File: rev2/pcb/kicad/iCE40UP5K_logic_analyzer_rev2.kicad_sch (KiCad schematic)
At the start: 117 parts, among them IC1 ICE40UP5K-SG48I, IC2 MIC5504-3.3YM5-TR, IC3 MIC5504-1.2YM5-TR, IC4 CP2102N-A02-GQFN24, IC5 W25Q40CLSNIG, IC6 SN74LVC14ADBRE4, IC7 SN74LVC14ADBRE4, IC8 SN74LVC14ADBRE4, J1 USB B Female Connector, J2 61300611121, J3 61202021621

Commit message: USB-UART bridge IC implementation. added LC filter to VPHY and VPLL. added caps to remaining power pins.
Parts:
- removed IC4: CP2102N-A02-GQFN24, UART_USB_bridge_CP2102N-A02-GQFN24:QFN50P400X400X80-25N-D, symbol UART_USB_bridge_CP2102N-A02-GQFN24:CP2102N-A02-GQFN24
- removed R8: 10k, Resistor_SMD:R_0603_1608Metric, symbol Device:R
- removed TP12, TP15: GND, TestPoint:TestPoint_Pad_D1.0mm, symbol Connector:TestPoint
- removed TP7: SPI_SCK, TestPoint:TestPoint_Pad_D1.0mm, symbol Connector:TestPoint
- removed TP8: FPGA_UART_TX, TestPoint:TestPoint_Pad_D1.0mm, symbol Connector:TestPoint
- removed TP9: FPGA_UART_RX, TestPoint:TestPoint_Pad_D1.0mm, symbol Connector:TestPoint
- added C27, C28, C29, C30, C31, C32, C33: 0u1, 0u1_0603_cap_C0603C104M4RAC:CAPC1608X95N, symbol Device:C
- added C34, C35: 4u7, 4u7_0805_cap_C0805C475K4RACTM:C0805, symbol Device:C
- added D8: USB_RX, Blue_LED_0805_APT2012LVBC/D:LEDC2012X85N, symbol Device:LED
- added D9: USB_TX, Yellow_LED_0805_150080YS75000:LEDC2012X70N, symbol Device:LED
- added FB1, FB2: BLM18AG601SN1D, BLM18SP221SN1B, symbol Ferrite_bead_BLM18AG601SN1D:BLM18AG601SN1D
- added IC4: FT2232HL-TRAY, QFP50P1200X1200X160-64N, symbol UART_USB_bridge_FT2232HL:FT2232HL-TRAY
- C6: value 4u7 -> 3u3
- R2: value 1k -> 12k
- R3: value 22k1 -> 10k
- R4: value 47k5 -> 4k7
- R5: value 10k -> 1k
- R6: value 10k -> 470R
- R7: value 10k -> 680R
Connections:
- net +3V3: now also R6.1, C28.2, C29.2, C30.1, C31.1, FB1.2, FB2.1, IC4.20 (VCCIO_1), IC4.31 (VCCIO_2), IC4.42 (VCCIO_3), IC4.50 (VREGIN), IC4.56 (VCCIO_4); no longer C6.1, C7.1, C8.1, R2.1, R6.2
- net +5V: now also R4.2; no longer R3.1
- net GND: now also R2.2, R3.1, C27.2, C28.1, C29.1, C30.2, C31.2, C32.1, C33.1, C34.2, C35.2, IC4.1 (GND_1), IC4.10 (AGND), IC4.11 (GND_3), IC4.13 (TEST), IC4.15 (GND_4), IC4.25 (GND_5), IC4.35 (GND_6), IC4.47 (GND_7), IC4.5 (GND_2), IC4.51 (GND_8), IC4.60 (PWREN#); no longer R4.2
- net at R5.2: now also IC4.14 (RESET#)
- net RTS#: now reaches IC1.2 (IOB_6A)
- net RTS#: now also IC4.18 (ADBUS2)
- net FPGA_UART_RX: now reaches IC1.3 (IOB_9B)
- net FPGA_UART_RX: now also IC4.16 (ADBUS0)
- net FPGA_UART_TX: now reaches IC1.4 (IOB_8A)
- net FPGA_UART_TX: now also IC4.17 (ADBUS1)
- net CTS#: now reaches IC1.6 (IOB_13B)
- net CTS#: now also IC4.19 (ADBUS3)
- net at R3.2, R4.1: now also IC4.59 (BCBUS7)
- net at R7.2: now also D9.2 (A)
- net USB_D+: now reaches D2.2 (K_2), J1.3
- net USB_D+: now also IC4.8 (DP)
- net USB_D-: now reaches D2.1 (K_1), J1.2
- net USB_D-: now also IC4.7 (DM)
- new net: D8.1 (K), IC4.29 (ACBUS3)
- new net: D8.2 (A), R6.2
- new net: D9.1 (K), IC4.30 (ACBUS4)
- new net: C33.2, C35.1, FB1.1, IC4.4 (VPHY)
- new net: IC4.6 (REF), R2.1
- new net: C32.2, C34.1, FB2.2, IC4.9 (VPLL)
- new net +1V8: C27.1, C6.1, C7.1, C8.1, IC4.12 (VCORE_1), IC4.37 (VCORE_2), IC4.49 (VREGOUT), IC4.64 (VCORE_3)
- no-connect marks 24 -> 36
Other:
- note added: "Integrated voltage regulator output"
- note added: "ring indicator control input"
- moved on the sheet: C1, C10, C24, C25, C26, IC6, IC7, IC8, R1, R15, R25, R26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

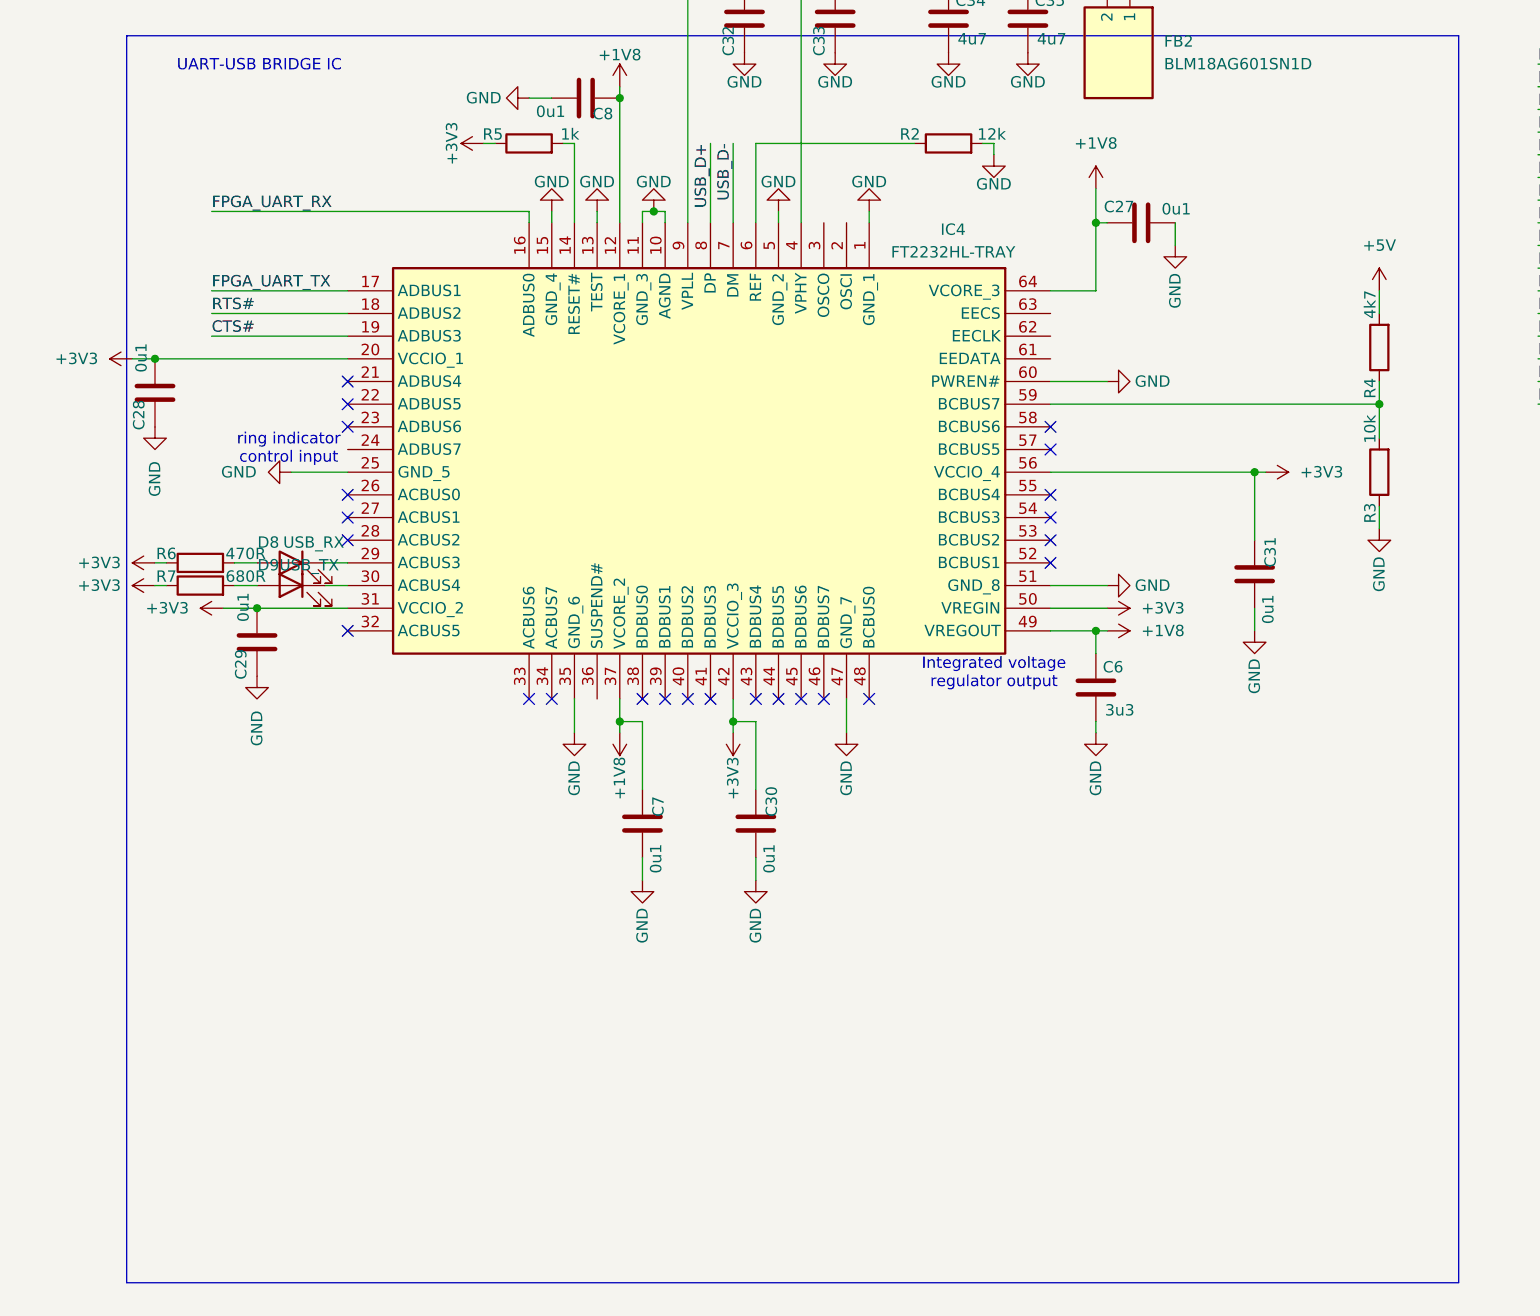
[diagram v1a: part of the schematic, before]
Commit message: bridge-IC finished in pcb schematic
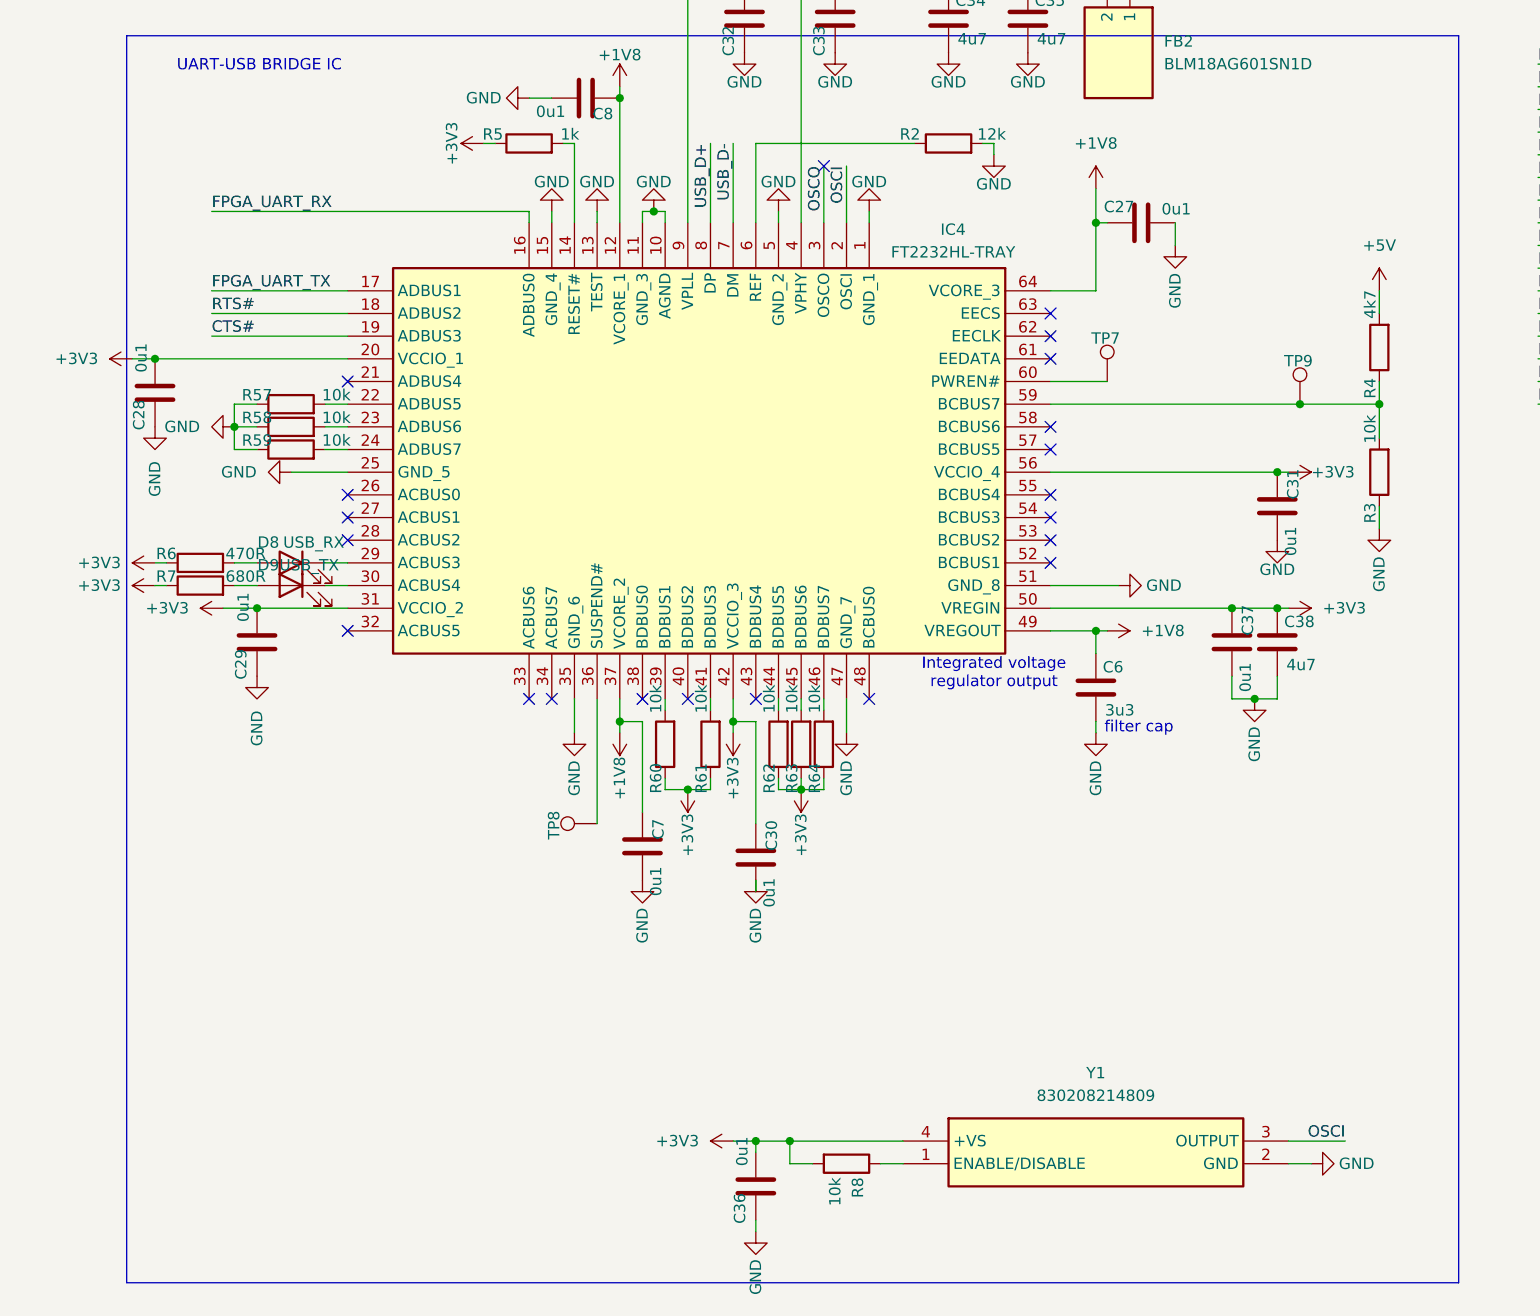
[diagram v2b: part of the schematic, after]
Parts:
- added C36, C37: 0u1, 0u1_0603_cap_C0603C104M4RAC:CAPC1608X95N, symbol Device:C
- added C38: 4u7, 4u7_0805_cap_C0805C475K4RACTM:C0805, symbol Device:C
- added R57, R58, R59, R60, R61, R62, R63, R64, R8: 10k, Resistor_SMD:R_0603_1608Metric, symbol Device:R
- added TP7: BRIDGE_PWREN#, TestPoint:TestPoint_Pad_D1.0mm, symbol Connector:TestPoint
- added TP8: BRIDGE_SUSPEND#, TestPoint:TestPoint_Pad_D1.0mm, symbol Connector:TestPoint
- added TP9: BRIDGE_PWRSAV#, TestPoint:TestPoint_Pad_D1.0mm, symbol Connector:TestPoint
- added Y1: 830208214809, 830208214809, symbol 12MHz_CMOS_clock_830208214809:830208214809
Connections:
- net +3V3: now also C36.2, C37.1, C38.1, R60.1, R61.1, R62.1, R63.1, R64.1, R8.2, Y1.4 (+VS)
- net GND: now also C36.1, C37.2, C38.2, R57.1, R58.1, R59.1, Y1.2 (GND); no longer IC4.60 (PWREN#)
- net OSCI: now reaches IC4.2 (OSCI)
- net OSCI: now also Y1.3 (OUTPUT)
- net at IC4.22 (ADBUS5): now also R57.2
- net at IC4.23 (ADBUS6): now also R58.2
- net at IC4.24 (ADBUS7): now also R59.2
- net OSCO: now reaches IC4.3 (OSCO)
- net at IC4.36 (SUSPEND#): now also TP8.1
- net at IC4.39 (BDBUS1): now also R60.2
- net at IC4.41 (BDBUS3): now also R61.2
- net at IC4.44 (BDBUS5): now also R62.2
- net at IC4.45 (BDBUS6): now also R63.2
- net at IC4.46 (BDBUS7): now also R64.2
- net at IC4.59 (BCBUS7), R3.2, R4.1: now also TP9.1
- new net: IC4.60 (PWREN#), TP7.1
- new net: R8.1, Y1.1 (ENABLE/DISABLE)
- no-connect marks 36 -> 33
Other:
- note added: "filter cap"
- note removed: "ring indicator control input"
- moved on the sheet: C30, C31, C7
